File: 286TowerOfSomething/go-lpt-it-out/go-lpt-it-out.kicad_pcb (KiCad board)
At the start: 2 copper layers, 42 parts, among them J1 Bus_ISA_8bit, J2 DE9, J3 Parallel, J4 Conn_02x05_Odd_Even, SW1 SW_DIP_x06, SW2 SW_DIP_x07, U1 TL16C552A, U2 GD75232N, U3 GD75232N, U4 74LS138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

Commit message: More work on layout
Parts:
- added Q1: MMBT3904, Package_TO_SOT_SMD:SOT-23, F.Cu at (253.6, 61.7)
- added R8: 1K, Resistor_SMD:R_0603_1608Metric_Pad0.98x0.95mm_HandSolder, F.Cu at (249.0, 60.6)
- added R9: 1K, Resistor_SMD:R_0603_1608Metric_Pad0.98x0.95mm_HandSolder, F.Cu at (249.0, 63.1)
- R4, R5, R6, R7: moved to B.Cu
- moved C2 184.3 mm to (76.2, 141.6), turned to 180 degrees
- moved C5 182.5 mm to (76.2, 140.0), turned to 180 degrees
- moved C10 171.9 mm to (84.5, 109.9), turned to 180 degrees
- moved C4 163.6 mm to (99.7, 154.9), turned to -90 degrees
- moved C16 162.7 mm to (98.6, 85.5), turned to 180 degrees
- moved C15 158.4 mm to (98.4, 109.9)
- moved C3 154.6 mm to (102.2, 118.2), turned to 90 degrees
- moved C6 142.7 mm to (113.7, 109.9), turned to 180 degrees
- moved C14 132.9 mm to (127.6, 87.0), turned to 180 degrees
- moved C13 128.9 mm to (127.6, 109.9)
- moved C19 59.5 mm to (177.8, 90.2), turned to 180 degrees
- moved U7 59.0 mm to (174.0, 92.7)
- moved U9 57.2 mm to (186.7, 92.7)
- moved C20 52.6 mm to (190.5, 90.2), turned to 180 degrees
- moved R4 48.7 mm to (176.5, 118.1), turned to 90 degrees
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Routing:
- net /Address and Config/~{0x278}: track 0.00 -> 22.5 mm
- net Net-(C8-Pad1): track 0.00 -> 15.8 mm
- net /Address and Config/~{0x2E8}: track 0.00 -> 14.4 mm
- net /Address and Config/~{0x3F8}: track 0.00 -> 11.5 mm
- net Net-(C7-Pad1): track 0.00 -> 11.0 mm
- net /Address and Config/~{0x378}: track 0.00 -> 10.3 mm
- net /Address and Config/~{0x3E8}: track 0.00 -> 9.73 mm
- net Net-(R2-Pad1): track 0.00 -> 7.93 mm
- net /Address and Config/~{0x3BC}: track 0.00 -> 6.66 mm
- net /Address and Config/~{UART1_CS}: track 0.00 -> 6.38 mm
- net /Address and Config/~{UART0_CS}: track 0.00 -> 6.31 mm
- net /Address and Config/~{0x2F8}: track 0.00 -> 5.41 mm
- net Net-(R2-Pad2): track 0.00 -> 4.97 mm
- net Net-(U6-Pad10): track 0.00 -> 3.89 mm
- net /CLK_UART: track 0.00 -> 2.98 mm
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
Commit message: More layout work on go-lpt-it-out
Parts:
- C2, C3, C4, C5: moved to B.Cu
- moved C2 11.5 mm to (87.6, 142.5), turned to 0 degrees
- moved C5 11.5 mm to (87.6, 140.8), turned to 0 degrees
- moved C4 11.3 mm to (99.7, 143.6), turned to 90 degrees
- moved C3 11.2 mm to (102.2, 129.4), turned to -90 degrees
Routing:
- net /D3: track 0.00 -> 74.8 mm, vias 0 -> 3
- net /D1: track 0.00 -> 74.8 mm, vias 0 -> 3
- net /D5: track 0.00 -> 73.5 mm, vias 0 -> 3
- net /D0: track 0.00 -> 72.0 mm, vias 0 -> 3
- net /D4: track 0.00 -> 71.8 mm, vias 0 -> 3
- net /D2: track 0.00 -> 71.8 mm, vias 0 -> 3
- net /D7: track 0.00 -> 71.3 mm, vias 0 -> 3
- net /D6: track 0.00 -> 69.2 mm, vias 0 -> 3
- net /A0: track 0.00 -> 66.2 mm, vias 0 -> 2
- net /PARPORT_SLCT: track 0.00 -> 65.8 mm, vias 0 -> 2
- net /A1: track 0.00 -> 65.7 mm, vias 0 -> 2
- net /PARPORT_PE: track 0.00 -> 64.6 mm, vias 0 -> 2
- net /A2: track 0.00 -> 58.6 mm, vias 0 -> 2
- net /PARPORT_BUSY: track 0.00 -> 58.1 mm, vias 0 -> 2
- net /~{PARPORT_ACK}: track 0.00 -> 56.4 mm, vias 0 -> 2
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
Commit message: More layout work on go-lpt-it-out
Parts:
- moved C18 171.5 mm to (44.5, 88.9), turned to -90 degrees
- moved U5 165.1 mm to (47.0, 92.7), turned to 90 degrees
- moved Q1 159.9 mm to (121.9, 152.4), turned to 90 degrees
- moved C17 159.2 mm to (44.5, 101.6), turned to -90 degrees
- moved R8 159.0 mm to (121.9, 156.2), turned to 180 degrees
- moved R9 153.1 mm to (121.9, 148.6)
- moved U4 152.9 mm to (47.0, 105.4), turned to 90 degrees
- moved SW1 149.5 mm to (68.6, 88.9), turned to 0 degrees
- moved C20 148.0 mm to (44.5, 114.3), turned to -90 degrees
- moved R6 146.5 mm to (72.4, 88.9), turned to 0 degrees
- moved U9 142.0 mm to (47.0, 118.1), turned to 90 degrees
- moved C19 138.3 mm to (44.5, 127.0), turned to -90 degrees
- moved R7 137.6 mm to (72.4, 96.5), turned to 0 degrees
- moved U7 132.6 mm to (47.0, 130.8), turned to 90 degrees
- moved SW2 123.2 mm to (68.6, 113.0), turned to 0 degrees
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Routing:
- net /Address and Config/A7: track 0.00 -> 108.1 mm, vias 0 -> 4
- net /Address and Config/A6: track 0.00 -> 99.3 mm, vias 0 -> 4
- net /Address and Config/A8: track 0.00 -> 96.7 mm, vias 0 -> 4
- net /Address and Config/A9: track 0.00 -> 84.0 mm, vias 0 -> 4
- net /Address and Config/A5: track 0.00 -> 78.0 mm
- net /~{UART0_RI}: track 0.00 -> 78.0 mm, vias 0 -> 1
- net /IRQ3: track 0.00 -> 76.4 mm, vias 0 -> 1
- net /~{UART0_CTS}: track 0.00 -> 75.0 mm, vias 0 -> 2
- net /~{UART0_DTR}: track 0.00 -> 71.0 mm, vias 0 -> 1
- net /IRQ4: track 0.00 -> 70.8 mm, vias 0 -> 1
- net /Address and Config/A3: track 0.00 -> 70.1 mm
- net /Address and Config/UART0_INT: track 0.00 -> 69.6 mm, vias 0 -> 1
- net /UART0_SOUT: track 3.96 -> 72.9 mm, vias 0 -> 2
- net /Address and Config/~{UART0_CS}: track 6.31 -> 74.5 mm
- net /~{UART0_DSR}: track 4.21 -> 71.4 mm, vias 0 -> 2
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
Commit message: Most of the layout done except for the power
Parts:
- moved C1 170.6 mm to (92.7, 116.0), turned to 90 degrees
- moved C9 167.2 mm to (97.8, 116.5), turned to 90 degrees
- moved R2 165.4 mm to (97.8, 113.0), turned to 90 degrees
- moved R3 164.0 mm to (97.8, 109.6), turned to 90 degrees
- moved U6 155.6 mm to (102.9, 113.0), turned to 180 degrees
- moved C12 155.3 mm to (109.9, 92.2), turned to 180 degrees
- moved C11 153.6 mm to (109.9, 99.1), turned to 180 degrees
- moved Y1 143.4 mm to (109.9, 115.5), turned to 90 degrees
- moved C7 137.0 mm to (113.7, 116.8), turned to -90 degrees
- moved R1 134.7 mm to (113.7, 113.0), turned to 90 degrees
- moved C8 132.8 mm to (113.7, 109.2), turned to 90 degrees
- moved C6 4.77 mm to (116.8, 113.4), turned to -90 degrees
- moved C16 4.45 mm to (94.1, 85.5)
- moved C15 4.44 mm to (94.0, 109.9)
- moved J4 4.44 mm to (99.8, 102.2)
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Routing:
- net /CLK_UART: track 2.98 -> 24.1 mm, vias 0 -> 2
- net /~{UART1_RI}: track 41.6 -> 46.3 mm
- net /~{UART1_DTR}: track 42.7 -> 47.0 mm
- net /~{UART1_DSR}: track 26.0 -> 30.1 mm
- net /UART1_SIN: track 47.5 -> 51.6 mm
- net /~{UART1_DCD}: track 24.2 -> 27.3 mm
- net /~{UART1_CTS}: track 36.3 -> 37.8 mm
- net /UART1_SOUT: track 30.8 -> 31.6 mm
- net /Address and Config/PEMD: track 46.7 -> 47.5 mm
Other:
- board text added: "0x278"
- board text added: "0x2E8"
- board text added: "0x2F8"
- board text added: "0x378"
- board text added: "0x3BC"
- board text added: "0x3E8"
- board text added: "0x3F8"
- board text added: "IRQ3"
- board text added: "IRQ4"
- board text added: "IRQ5"
- board text added: "IRQ6"
- board text added: "IRQ7"
- board text added: "PEMD"

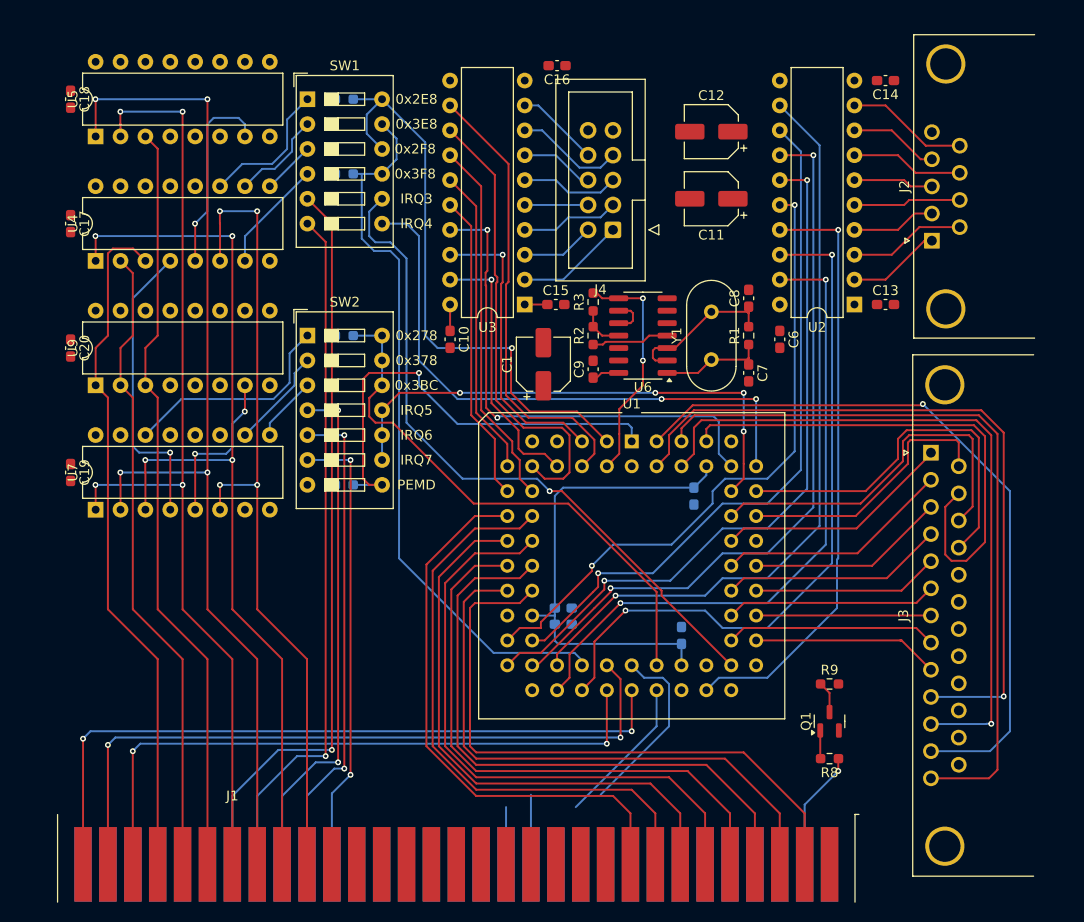
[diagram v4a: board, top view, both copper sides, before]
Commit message: Added a board edge to go-lpt-it-out and almost finished routing
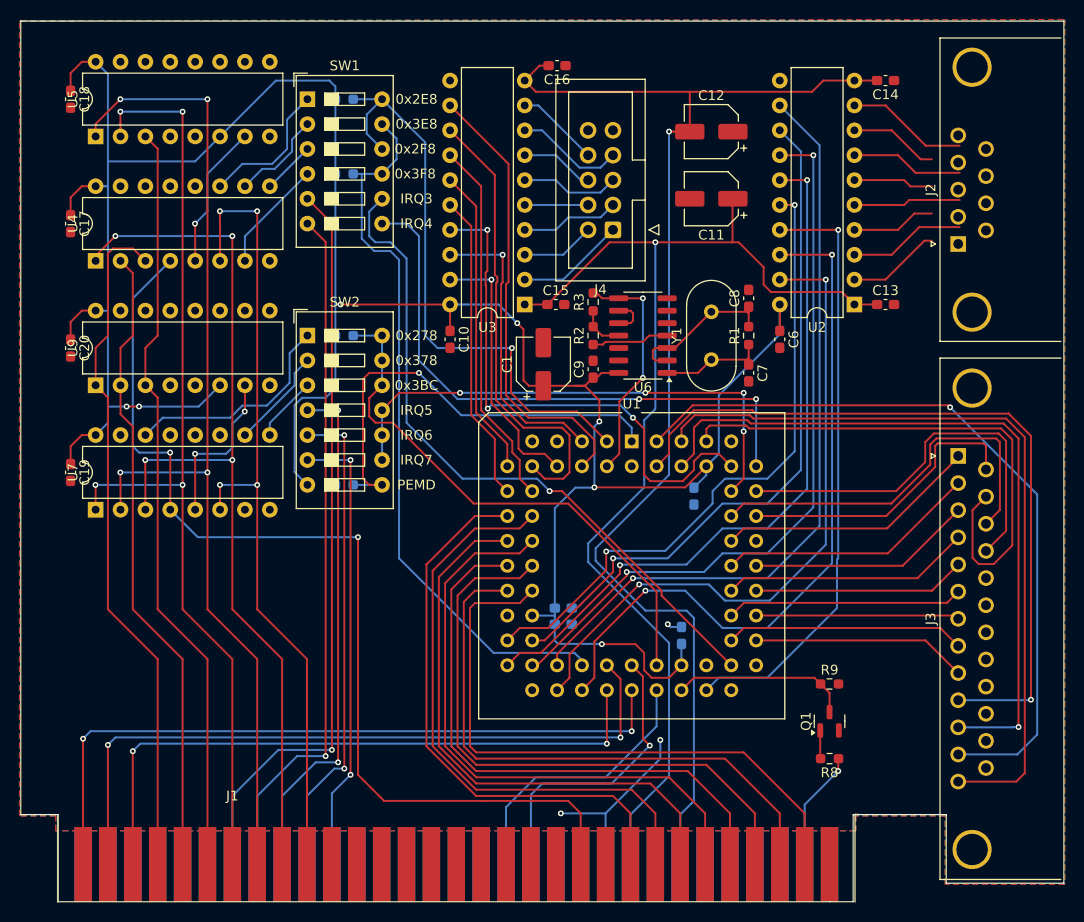
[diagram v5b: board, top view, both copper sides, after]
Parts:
- moved J3 2.80 mm to (135.1, 125.3)
- moved J2 2.70 mm to (135.1, 103.7)
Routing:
- net +5V: track 55.3 -> 271.9 mm, vias 0 -> 7
- net -12V: track 0.00 -> 131.3 mm, vias 0 -> 1
- net +12V: track 2.31 -> 118.1 mm, vias 0 -> 1
- net /Address and Config/AEN: track 30.4 -> 104.6 mm, vias 1 -> 2
- net GND: track 0.00 -> 21.1 mm, vias 0 -> 3
- net /~{RESET}: track 3.25 -> 18.2 mm
- net /~{IOR}: track 21.2 -> 28.3 mm
- net Net-(U4-E2): track 20.1 -> 14.8 mm
- net /~{IOW}: track 25.9 -> 30.3 mm, vias 0 -> 1
- net /UART1_SIN: track 51.6 -> 55.4 mm, vias 2 -> 3
- net /PARPORT_PE: track 74.7 -> 77.7 mm
- net /~{PARPORT_ACK}: track 74.2 -> 77.2 mm
- net /PARPORT_PD5: track 17.9 -> 20.8 mm
- net /PARPORT_SLCT: track 76.4 -> 79.3 mm
- net /PARPORT_BUSY: track 71.4 -> 74.3 mm
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- added copper zone on B.Cu, net GND
- added copper zone on F.Cu, net GND
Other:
- board outline added: 106.5 x 89.9 mm

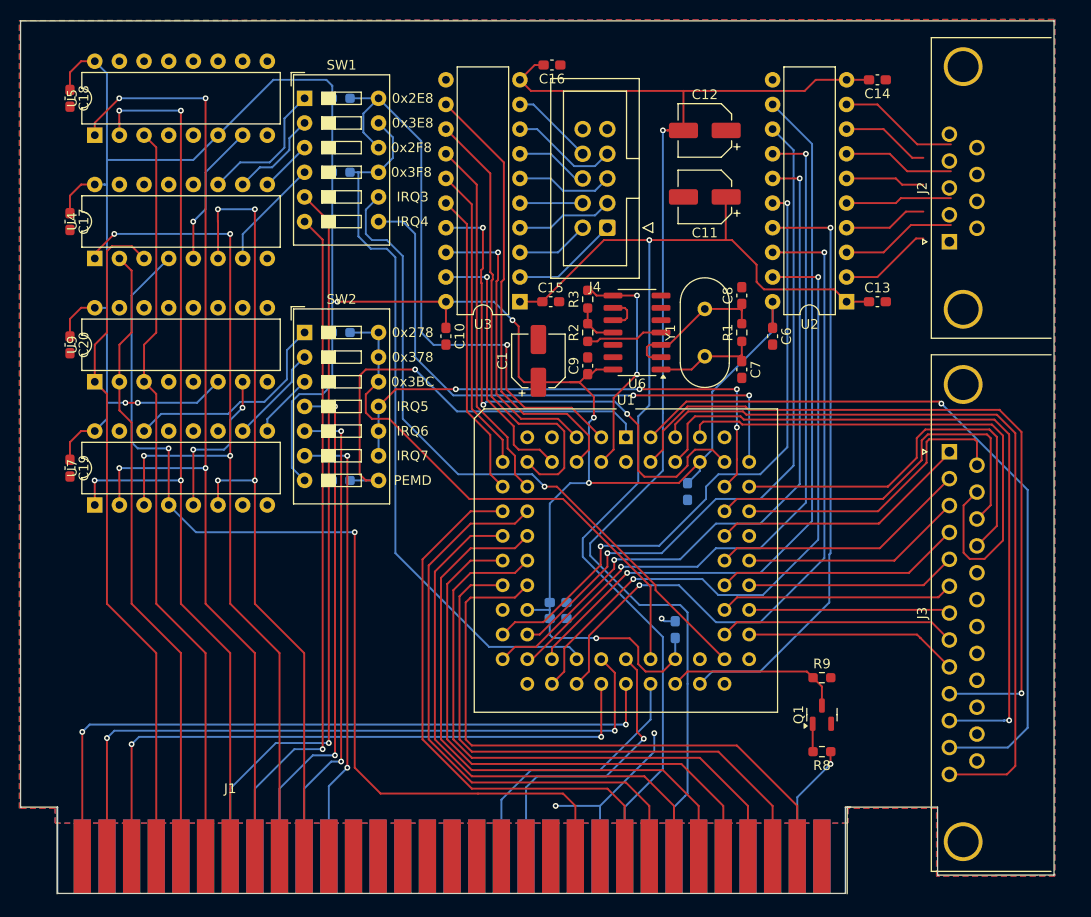
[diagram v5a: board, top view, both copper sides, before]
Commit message: Updating go-lpt-it-out with bracket
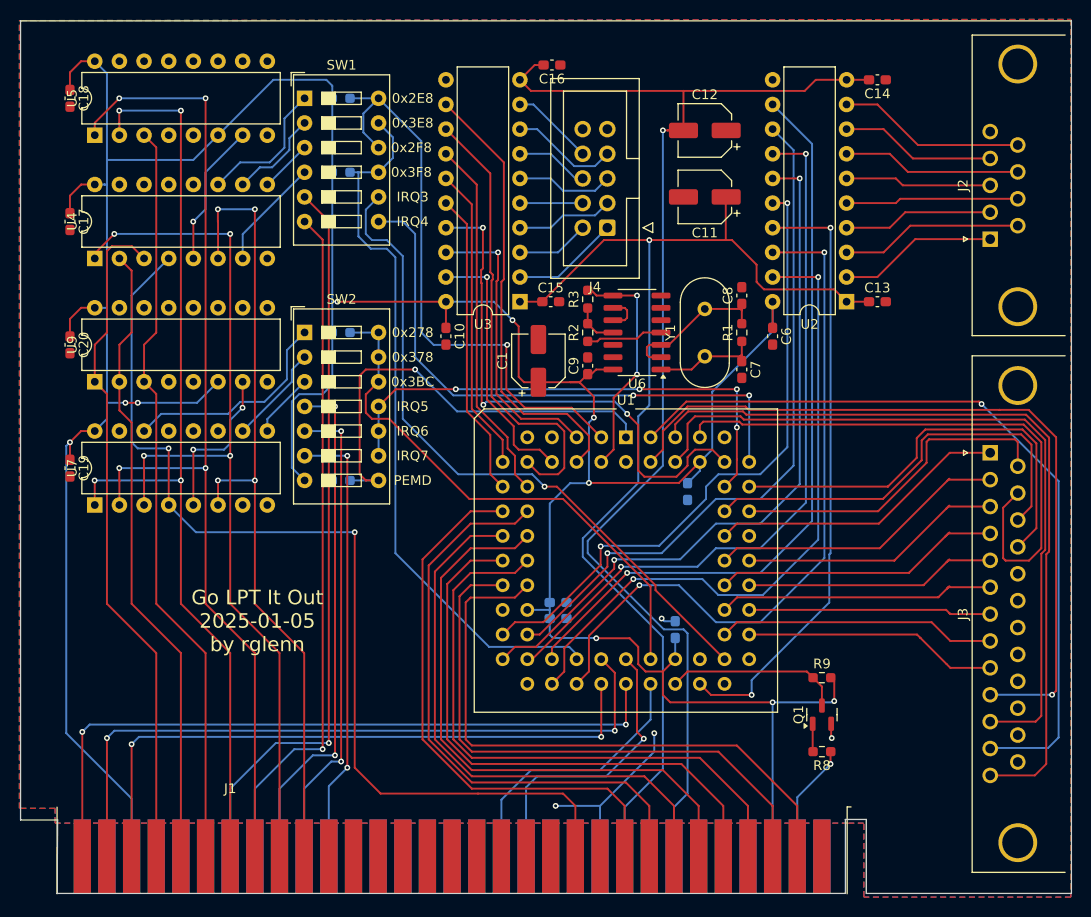
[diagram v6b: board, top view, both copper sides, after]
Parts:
- added BRACKET1: ~, pc-parts:PC_BRACKET_ISA_KEYSTONE_9200_Rev1_1, F.Cu at (121.9, 170.8)
- J2: footprint Connector_Dsub:DSUB-9_Male_Horizontal_P2.77x2.84mm_EdgePinOffset7.70mm_Housed_MountingHolesOffset9.12mm -> Connector_Dsub:DSUB-9_Male_Horizontal_P2.77x2.84mm_EdgePinOffset4.94mm_Housed_MountingHolesOffset4.94mm
- J3: footprint Connector_Dsub:DSUB-25_Female_Horizontal_P2.77x2.84mm_EdgePinOffset7.70mm_Housed_MountingHolesOffset9.12mm -> Connector_Dsub:DSUB-25_Female_Horizontal_P2.77x2.84mm_EdgePinOffset4.94mm_Housed_MountingHolesOffset4.94mm
- moved J2 4.21 mm to (139.3, 103.4)
- moved J3 4.21 mm to (139.3, 125.4)
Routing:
- net +5V: track 271.9 -> 356.4 mm, vias 7 -> 10
- net Net-(U2-RA5): track 12.5 -> 19.4 mm
- net Net-(U2-DY2): track 8.18 -> 15.1 mm
- net Net-(U2-DY3): track 9.13 -> 16.0 mm
- net Net-(U2-RA4): track 11.5 -> 18.4 mm
- net Net-(U2-RA1): track 9.56 -> 16.4 mm
- net Net-(U2-DY1): track 11.0 -> 17.8 mm
- net Net-(U2-RA2): track 11.9 -> 18.8 mm
- net Net-(U2-RA3): track 8.60 -> 15.5 mm
- net /PARPORT_PD2: track 25.4 -> 30.1 mm
- net /PARPORT_PD1: track 23.0 -> 27.6 mm
- net /PARPORT_PD3: track 21.7 -> 26.3 mm
- net /PARPORT_PD4: track 24.2 -> 28.7 mm
- net /PARPORT_PD0: track 26.7 -> 31.1 mm
- net /~{PARPORT_ERR}: track 56.0 -> 60.3 mm
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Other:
- board size 106.5 x 89.9 mm -> 108.3 x 89.9 mm
- board text added: "Go LPT It Out 2025-01-05 by rglenn"
